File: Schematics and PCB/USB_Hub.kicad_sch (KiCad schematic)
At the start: 91 parts, among them J4 DOWNSTREAM_1, J5 UPSTREAM, J7 DOWNSTREAM_3, J8 DOWNSTREAM_1, U16 TUSB8042A, U17 TPS2561, U18 TPS2561, U19 TLV71311PDBVR, U20 TLV70033DDCR, Y1 24MHz 20pF GND24

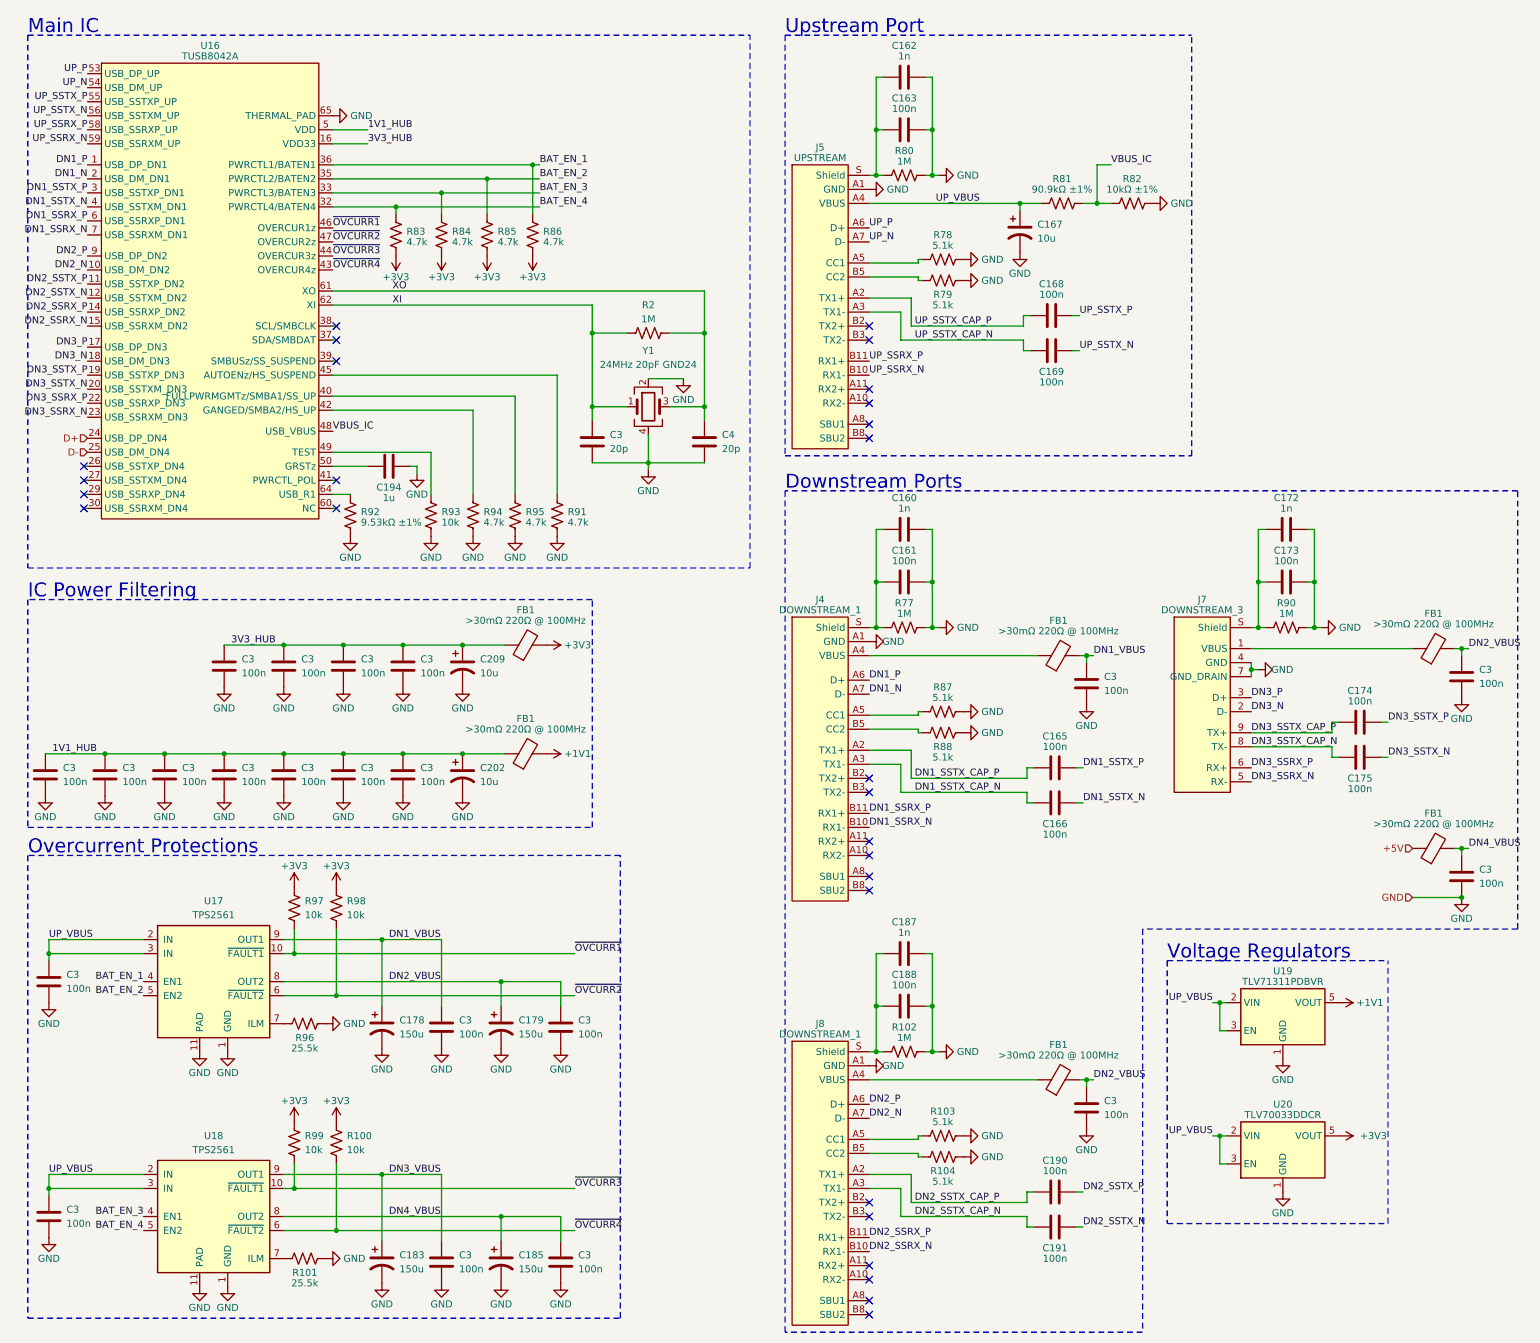
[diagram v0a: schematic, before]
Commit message: Updated USB hub
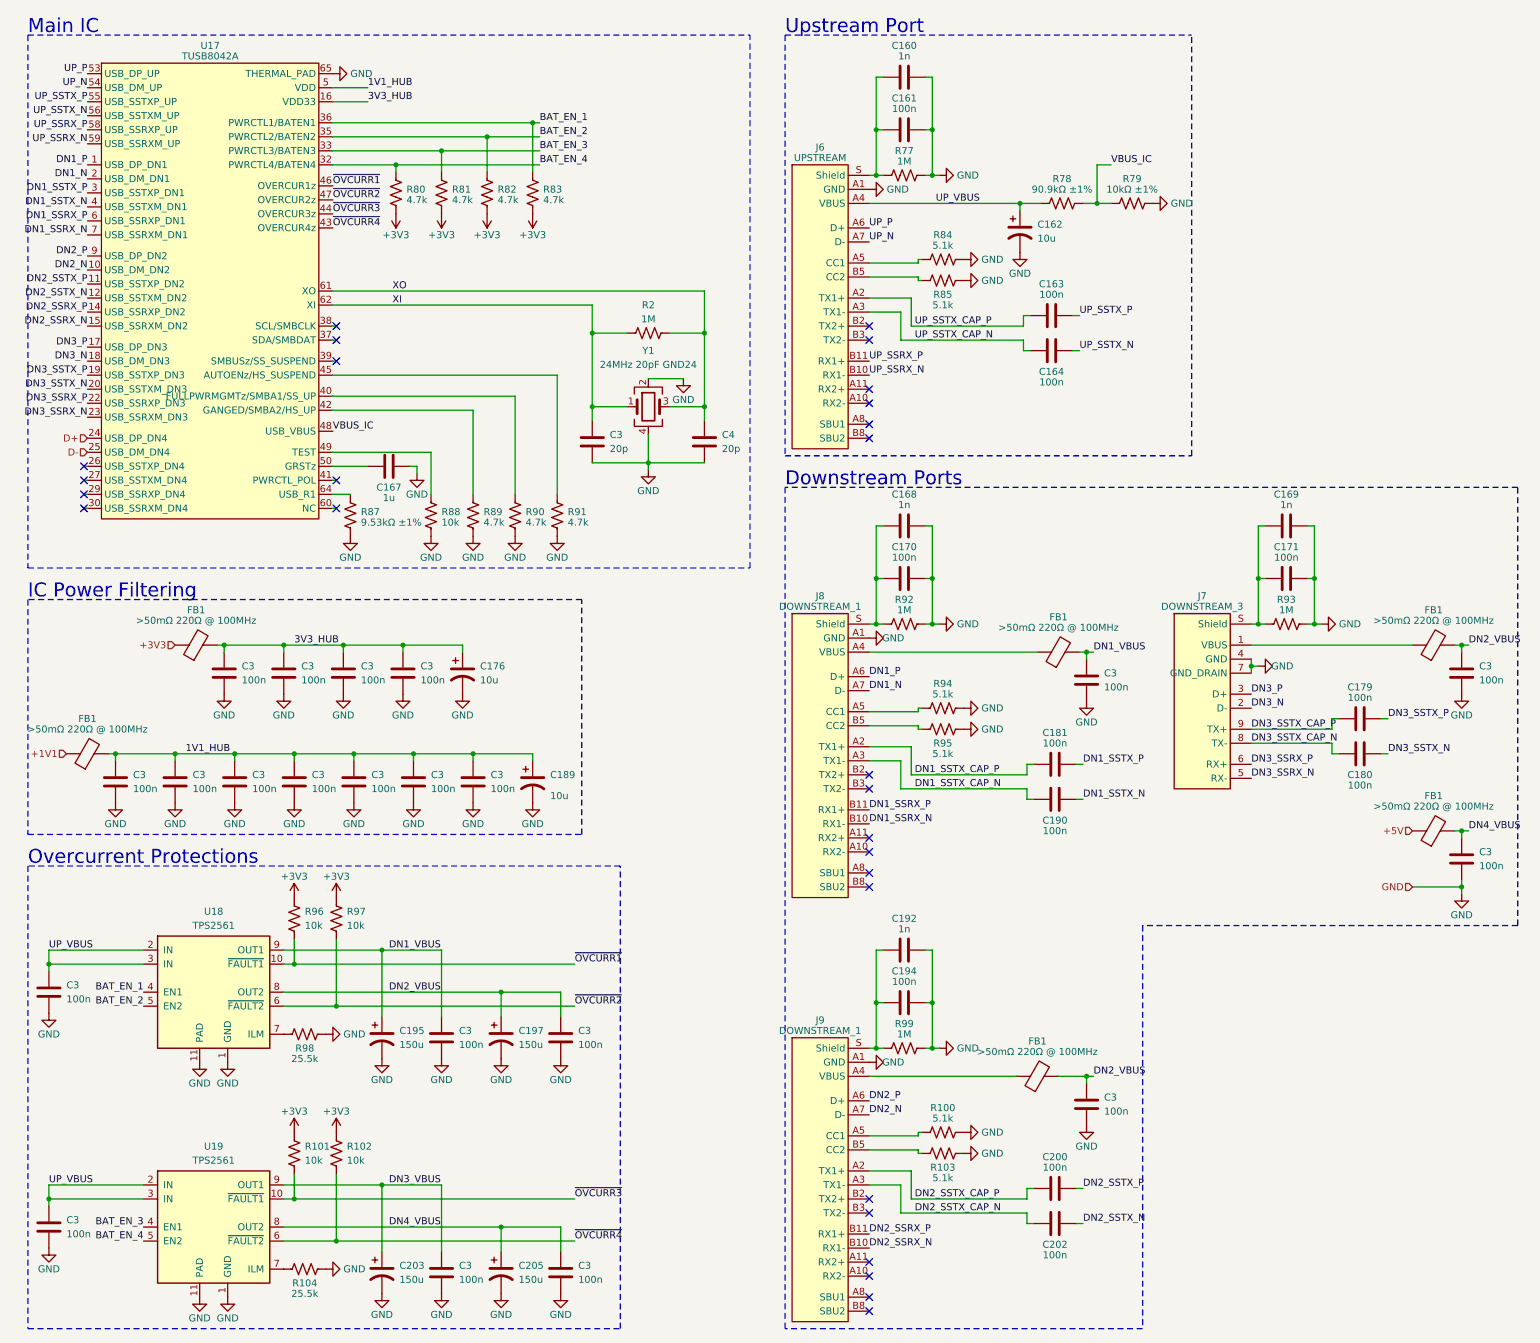
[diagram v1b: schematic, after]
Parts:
- removed FB1 (x2): >30mΩ 220Ω @ 100MHz, symbol Device:FerriteBead
- removed R84, R85, R86: 4.7k, symbol Device:R_US
- removed U19: TLV71311PDBVR, Package_TO_SOT_SMD:TSOT-23-5, symbol Regulator_Linear:ADP7182AUJZ-1.8
- removed U20: TLV70033DDCR, Package_TO_SOT_SMD:TSOT-23-5, symbol Regulator_Linear:ADP7182AUJZ-1.8
- added FB1 (x2): >50mΩ 220Ω @ 100MHz, symbol Device:FerriteBead
- added R80, R81, R82: 4.7k, symbol Device:R_US
- FB1: value >30mΩ 220Ω @ 100MHz -> >50mΩ 220Ω @ 100MHz
- R2: footprint (none) -> Resistor_SMD:R_0603_1608Metric
- R77: renamed from R80; footprint (none) -> Resistor_SMD:R_0603_1608Metric
- R92: renamed from R77; footprint (none) -> Resistor_SMD:R_0603_1608Metric
- R93: renamed from R90; footprint (none) -> Resistor_SMD:R_0603_1608Metric
- R99: renamed from R102; footprint (none) -> Resistor_SMD:R_0603_1608Metric
- renumbered C162 to C160, C163 to C161, C167 to C162, C168 to C163, C169 to C164, C194 to C167, C160 to C168, C172 to C169, C161 to C170, C173 to C171, C209 to C176, C174 to C179, C175 to C180, C165 to C181, C202 to C189, C166 to C190, C187 to C192, C188 to C194, C178 to C195, C179 to C197, C190 to C200, C191 to C202, C183 to C203, C185 to C205, J5 to J6, J4 to J8, J8 to J9, R103 to R100, R99 to R101, R100 to R102, R104 to R103, R101 to R104, R81 to R78, R82 to R79, R78 to R84, R79 to R85, R92 to R87, R93 to R88, R94 to R89, R95 to R90, R87 to R94, R88 to R95, R97 to R96, R98 to R97, R96 to R98, U16 to U17, U17 to U18, U18 to U19
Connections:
- net +1V1: now also FB1.1
- net +3V3: now also FB1.1, R80.2, R81.2, R82.2
- net 1V1_HUB: now also FB1.2
- net 3V3_HUB: now also FB1.2
- net BAT_EN_1: now also R83.1
- net BAT_EN_2: now also R82.1
- net BAT_EN_3: now also R81.1
- net BAT_EN_4: now also R80.1; no longer R83.1
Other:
- note removed: "Voltage Regulators"
- moved on the sheet: C168, C169, C170, C171, C176, C179, C180, C181, C189, C190, C192, C194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

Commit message: Pre initial PCB layout commit
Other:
- moved on the sheet: C3, C4
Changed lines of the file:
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@@
     (stroke (width 0) (type default))
   )
-  (wire (pts (xy 129.54 89.535) (xy 129.54 94.615))
-    (stroke (width 0) (type default))
-  )
   (wire (pts (xy 90.17 100.33) (xy 90.17 92.71))
     (stroke (width 0) (type default))
@@
     (stroke (width 0) (type default))
   )
+  (wire (pts (xy 139.7 94.615) (xy 139.7 93.345))
+    (stroke (width 0) (type default))
+  )
   (wire (pts (xy 210.82 47.625) (xy 213.36 47.625))
     (stroke (width 0) (type default))
@@
     (stroke (width 0) (type default))
   )
-  (wire (pts (xy 139.7 84.455) (xy 139.7 86.995))
+  (wire (pts (xy 139.7 84.455) (xy 139.7 85.725))
     (stroke (width 0) (type default))
   )
@@
     (stroke (width 0) (type dash))
   )
+  (wire (pts (xy 119.38 94.615) (xy 119.38 93.345))
+    (stroke (width 0) (type default))
+  )
   (wire (pts (xy 177.165 69.85) (xy 197.485 69.85))
     (stroke (width 0) (type default))
@@
     (stroke (width 0) (type default))
   )
+  (wire (pts (xy 129.54 89.535) (xy 129.54 94.615))
+    (stroke (width 0) (type default))
+  )
   (wire (pts (xy 86.995 147.32) (xy 97.79 147.32))
     (stroke (width 0) (type default))
@@
     (stroke (width 0) (type default))
   )
-  (wire (pts (xy 119.38 84.455) (xy 119.38 86.995))
+  (wire (pts (xy 119.38 84.455) (xy 119.38 85.725))
     (stroke (width 0) (type default))
   )
@@
     )
   )
-  (symbol (lib_id "Device:C") (at 119.38 90.805 0) (unit 1)
+  (symbol (lib_id "Device:C") (at 119.38 89.535 0) (unit 1)
     (in_bom yes) (on_board yes) (dnp no)
-    (property "Reference" "C3" (at 122.555 89.535 0)
+    (property "Reference" "C3" (at 122.555 88.265 0)
       (effects (font (size 1.27 1.27)) (justify left))
     )
-    (property "Value" "20p" (at 122.555 92.075 0)
+    (property "Value" "20p" (at 122.555 90.805 0)
       (effects (font (size 1.27 1.27)) (justify left))
     )
-    (property "Footprint" "" (at 120.3452 94.615 0)
+    (property "Footprint" "" (at 120.3452 93.345 0)
       (effects (font (size 1.27 1.27)) hide)
     )
-    (property "Datasheet" "~" (at 119.38 90.805 0)
+    (property "Datasheet" "~" (at 119.38 89.535 0)
       (effects (font (size 1.27 1.27)) hide)
     )
@@
       (effects (font (size 1.27 1.27)) (justify left))
     )
-    (property "Value" "10u" (at 111.76 154.94 0)
+    (property "Value" "10u" (at 111.76 153.67 0)
       (effects (font (size 1.27 1.27)) (justify left))
     )
@@
     )
   )
-  (symbol (lib_id "Device:C") (at 139.7 90.805 0) (unit 1)
+  (symbol (lib_id "Device:C") (at 139.7 89.535 0) (unit 1)
     (in_bom yes) (on_board yes) (dnp no)
-    (property "Reference" "C4" (at 142.875 89.535 0)
+    (property "Reference" "C4" (at 142.875 88.265 0)
       (effects (font (size 1.27 1.27)) (justify left))
     )
-    (property "Value" "20p" (at 142.875 92.075 0)
+    (property "Value" "20p" (at 142.875 90.805 0)
       (effects (font (size 1.27 1.27)) (justify left))
     )
-    (property "Footprint" "" (at 140.6652 94.615 0)
+    (property "Footprint" "" (at 140.6652 93.345 0)
       (effects (font (size 1.27 1.27)) hide)
     )
-    (property "Datasheet" "~" (at 139.7 90.805 0)
+    (property "Datasheet" "~" (at 139.7 89.535 0)
       (effects (font (size 1.27 1.27)) hide)
     )

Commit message: minor changes
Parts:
- removed C160, C168, C169, C192: 1n, symbol Device:C
- removed C161, C170, C171, C179, C180, C181, C190, C194, C200, C202, C3 (x5): 100n, symbol Device:C
- removed C3: 20p, symbol Device:C
- removed FB1 (x4): >50mΩ 220Ω @ 100MHz, symbol Device:FerriteBead
- removed J7: DOWNSTREAM_3, symbol mechpadLibrary:USB_A_Receptacle
- removed J9: DOWNSTREAM_1, symbol mechpadLibrary:USB_C_Receptacle
- removed R100, R103, R84, R85, R94, R95: 5.1k, symbol Device:R_US
- removed R77, R92, R93, R99: 1M, Resistor_SMD:R_0603_1608Metric, symbol Device:R_US
- removed R78: 90.9kΩ ±1%, symbol Device:R_US
- removed R79: 10kΩ ±1%, symbol Device:R_US
- added C1, C2: 20p, symbol Device:C
- added C10, C12, C130, C133, C134, C15, C5, C7: 100n, symbol Device:C
- added C101, C11, C3, C6: 1n, symbol Device:C
- added C13, C131, C132, C14, C8, C9: 100n, Capacitor_SMD:C_0201_0603Metric, symbol Device:C
- added D120: DESD5V0U1BA, Diode_SMD:D_SOD-323_HandSoldering, symbol Device:D_TVS
- added D121: B240A-13-F, Diode_SMD:D_SMA, symbol Diode:1N4148W
- added F2: 2A, Fuse:Fuse_1812_4532Metric, symbol Device:Polyfuse
- added FB1, FB2, FB3, FB4: >50mΩ 220Ω @ 100MHz, symbol Device:FerriteBead
- added J3, J4: DOWNSTREAM_1, symbol mechpadLibrary:USB_C_Receptacle
- added R1: 4.7k, symbol Device:R_US
- added R10, R11, R12, R32, R5, R53, R6, R9: 5.1k, symbol Device:R_US
- added R2: 90.9kΩ ±1%, Resistor_SMD:R_0402_1005Metric, symbol Device:R_US
- added R3: 10kΩ ±1%, Resistor_SMD:R_0402_1005Metric, symbol Device:R_US
- added R31, R4, R7, R8: 1M, Resistor_SMD:R_0603_1608Metric, symbol Device:R_US
- C163, C164: footprint (none) -> Capacitor_SMD:C_0201_0603Metric
- C4: value 20p -> 100n
- Y1: value 24MHz 20pF GND24 -> 24MHz; Additional req. (none) -> Max 50R ESR
- renumbered C3 to C172, C3 to C173, C3 to C174, C3 to C175, C3 to C182, C3 to C183, C3 to C184, C3 to C185, C3 to C186, C3 to C187, C3 to C188, C3 to C193, C3 to C196, C3 to C198, C3 to C204, C3 to C206, FB1 to FB10, FB1 to FB7, R2 to R86
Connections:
- net +3V3: now also R1.2
- net DN1_SSTX_CAP_N: now also C9.1
- net DN1_SSTX_CAP_P: now also C8.1
- net DN1_SSTX_N: now also C9.2
- net DN1_SSTX_P: now also C8.2
- net DN1_VBUS: now also C10.1, FB1.2
- net DN2_N: now also J3.A7 (D-)
- net DN2_P: now also J3.A6 (D+), J3.B6 (D+)
- net DN2_SSRX_N: now also J3.B10 (RX1-)
- net DN2_SSRX_P: now also J3.B11 (RX1+)
- net DN2_SSTX_CAP_N: now also C14.1, J3.A3 (TX1-)
- net DN2_SSTX_CAP_P: now also C13.1, J3.A2 (TX1+)
- net DN2_SSTX_N: now also C14.2
- net DN2_SSTX_P: now also C13.2
- net DN2_VBUS: now also C12.1, FB2.2
- net DN3_N: now also J4.A7 (D-)
- net DN3_P: now also J4.A6 (D+), J4.B6 (D+)
- net DN3_SSRX_N: now also J4.B10 (RX1-)
- net DN3_SSRX_P: now also J4.B11 (RX1+)
- net DN3_SSTX_CAP_N: now also C132.1, J4.A3 (TX1-)
- net DN3_SSTX_CAP_P: now also C131.1, J4.A2 (TX1+)
- net DN3_SSTX_N: now also C132.2
- net DN3_SSTX_P: now also C131.2
- net DN3_VBUS: now also C130.1, FB3.2
- net DN4_VBUS: now also C134.1, FB4.2
- net GND: now also C1.1, C10.2, C101.2, C11.2, C12.2, C130.2, C133.2, C134.2, C15.2, C2.1, C3.2, C5.2, C6.2, C7.2, D120.1 (A1), J3.A1 (GND), J3.A12 (GND), J4.A1 (GND), J4.A12 (GND), R10.2, R11.1, R12.1, R3.2, R31.2, R32.2, R4.2, R5.2, R53.1, R6.1, R7.2, R8.2, R9.2
- net UP_VBUS: now also C133.1, D121.1 (K), F2.1, R2.1
- net VBUS_IC: now also R2.2, R3.1
- net XI: now also C2.2
- net XO: now also C1.2; no longer C4.1
- net at J8.B5 (CC2): now also R11.2
- net GNDS: now reaches J8.S (Shield)
- net GNDS: now also C4.1, J6.S (Shield), C101.1, C11.1, C15.1, C3.1, C5.1, C6.1, C7.1, J3.S (Shield), J4.S (Shield), R31.1, R4.1, R7.1, R8.1
- net at J6.A5 (CC1): now also R5.1
- net at J6.B5 (CC2): now also R6.2
- net at J8.A5 (CC1): now also R10.1
- net at U17.41 (PWRCTL_POL): now also R1.1
- net DN1_VBUS_FB: now reaches J8.A4 (VBUS), J8.A9 (VBUS)
- net DN1_VBUS_FB: now also FB1.1
- new net: J3.A5 (CC1), R9.1
- new net: J3.B1 (GND), J3.B12 (GND)
- new net: J3.B4 (VBUS), J3.B9 (VBUS)
- new net: J3.B5 (CC2), R12.2
- new net: J4.B5 (CC2), R53.2
- new net: J4.A5 (CC1), R32.1
- new net: J4.B1 (GND), J4.B12 (GND)
- new net: J4.B4 (VBUS), J4.B9 (VBUS)
- new net 5V fused: D120.2 (A2), D121.2 (A), F2.2
- new net DN2_VBUS_FB: FB2.1, J3.A4 (VBUS), J3.A9 (VBUS)
- new net DN3_VBUS_FB: FB3.1, J4.A4 (VBUS), J4.A9 (VBUS)
- new net DN4_VCC: FB4.1
- no-connect marks 27 -> 32
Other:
- note added: "Downstream Port 1"
- note added: "Downstream Port 2"
- note added: "Downstream Port 3"
- note added: "Downstream Port 4 (microcontroller)"
- note removed: "Downstream Ports"
- moved on the sheet: C162, C163, C164, C167, C172, C173, C174, C175, C176, C182, C183, C184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
